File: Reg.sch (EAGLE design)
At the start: 12 parts, among them Q1 NPN2SC3422-2, Q2 NPN2SC3325, Q3 PNP2SA1313

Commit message: 完成
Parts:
- D1: value RED -> SHORT
- D2: value BLUE -> SHORT
- D3, D4: value (none) -> BLUE
- R1, R4: value 1k -> 1.5k
- R2: value DNP -> 1.5k
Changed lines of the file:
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@@
 <part name="Q2" library="my_ic" deviceset="NPN" device="2SC3325"/>
 <part name="JP1" library="pinhead" library_urn="urn:adsk.eagle:library:325" deviceset="PINHD-1X3" device="" package3d_urn="urn:adsk.eagle:package:22458/2" value="CON"/>
-<part name="D1" library="my_rcl" deviceset="LED" device="-SMD1608" value="RED"/>
-<part name="D2" library="my_rcl" deviceset="LED" device="-SMD1608" value="BLUE"/>
-<part name="R2" library="my_rcl" deviceset="R" device="-1608" value="DNP"/>
+<part name="D1" library="my_rcl" deviceset="LED" device="-SMD1608" value="SHORT"/>
+<part name="D2" library="my_rcl" deviceset="LED" device="-SMD1608" value="SHORT"/>
+<part name="R2" library="my_rcl" deviceset="R" device="-1608" value="1.5k"/>
 <part name="Q3" library="my_ic" deviceset="PNP" device="2SA1313"/>
-<part name="R1" library="my_rcl" deviceset="R" device="-1608" value="1k"/>
-<part name="R4" library="my_rcl" deviceset="R" device="-1608" value="1k"/>
+<part name="R1" library="my_rcl" deviceset="R" device="-1608" value="1.5k"/>
+<part name="R4" library="my_rcl" deviceset="R" device="-1608" value="1.5k"/>
 <part name="C7" library="my_rcl" deviceset="C" device="-1608" value="100p"/>
-<part name="D3" library="my_rcl" deviceset="LED" device="-SMD1608"/>
-<part name="D4" library="my_rcl" deviceset="LED" device="-SMD1608"/>
+<part name="D3" library="my_rcl" deviceset="LED" device="-SMD1608" value="BLUE"/>
+<part name="D4" library="my_rcl" deviceset="LED" device="-SMD1608" value="BLUE"/>
 </parts>
 <sheets>
@@
 </instance>
 <instance part="D1" gate="G$1" x="15.24" y="5.08" smashed="yes">
-<attribute name="NAME" x="11.176" y="0.508" size="1.778" layer="95" rot="R90"/>
-<attribute name="VALUE" x="10.795" y="5.588" size="1.778" layer="96" rot="R90"/>
+<attribute name="NAME" x="11.176" y="-2.032" size="1.778" layer="95" rot="R90"/>
+<attribute name="VALUE" x="10.795" y="3.048" size="1.778" layer="96" rot="R90"/>
 </instance>
 <instance part="D2" gate="G$1" x="22.86" y="5.08" smashed="yes">
-<attribute name="NAME" x="26.416" y="0.508" size="1.778" layer="95" rot="R90"/>
-<attribute name="VALUE" x="26.035" y="4.318" size="1.778" layer="96" rot="R90"/>
+<attribute name="NAME" x="26.416" y="-2.032" size="1.778" layer="95" rot="R90"/>
+<attribute name="VALUE" x="26.035" y="3.048" size="1.778" layer="96" rot="R90"/>
 </instance>
 <instance part="R2" gate="G$1" x="30.48" y="5.08" smashed="yes" rot="R90">
@@
 </instance>
 <instance part="R1" gate="G$1" x="7.62" y="25.4" smashed="yes" rot="R90">
-<attribute name="NAME" x="6.1214" y="22.86" size="1.778" layer="95" rot="R90"/>
-<attribute name="VALUE" x="10.922" y="21.59" size="1.778" layer="96" rot="R90"/>
+<attribute name="NAME" x="11.2014" y="19.05" size="1.778" layer="95" rot="R90"/>
+<attribute name="VALUE" x="10.922" y="22.86" size="1.778" layer="96" rot="R90"/>
 </instance>
 <instance part="R4" gate="G$1" x="2.54" y="27.94" smashed="yes" rot="R90">
 <attribute name="NAME" x="1.0414" y="24.13" size="1.778" layer="95" rot="R90"/>
-<attribute name="VALUE" x="5.842" y="24.13" size="1.778" layer="96" rot="R90"/>
+<attribute name="VALUE" x="0.762" y="27.94" size="1.778" layer="96" rot="R90"/>
 </instance>
 <instance part="C7" gate="G$1" x="22.86" y="20.32" smashed="yes">

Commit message: チップオンリーも
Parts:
- added Q4: NPN2SC3325, my_ic:NPN2SC3325
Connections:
- net IN: now also Q4.C
- net N$1: now also Q4.B
- net OUT: now also Q4.E
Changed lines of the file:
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@@
 <part name="D3" library="my_rcl" deviceset="LED" device="-SMD1608" value="BLUE"/>
 <part name="D4" library="my_rcl" deviceset="LED" device="-SMD1608" value="BLUE"/>
+<part name="Q4" library="my_ic" deviceset="NPN" device="2SC3325"/>
 </parts>
 <sheets>
@@
 <attribute name="VALUE" x="36.195" y="25.908" size="1.778" layer="96" rot="R90"/>
 </instance>
+<instance part="Q4" gate="G$1" x="15.24" y="40.64" smashed="yes" rot="R90">
+<attribute name="NAME" x="15.24" y="45.72" size="1.778" layer="95" rot="R90"/>
+<attribute name="VALUE" x="17.78" y="45.72" size="1.778" layer="96" rot="R90"/>
+</instance>
 </instances>
 <busses>
@@
 <wire x1="50.8" y1="-7.62" x2="50.8" y2="33.02" width="0.1524" layer="91"/>
 <pinref part="Q1" gate="G$1" pin="E"/>
-<wire x1="20.32" y1="33.02" x2="30.48" y2="33.02" width="0.1524" layer="91"/>
+<wire x1="20.32" y1="33.02" x2="22.86" y2="33.02" width="0.1524" layer="91"/>
 <pinref part="D4" gate="G$1" pin="A"/>
+<wire x1="22.86" y1="33.02" x2="30.48" y2="33.02" width="0.1524" layer="91"/>
 <wire x1="30.48" y1="33.02" x2="50.8" y2="33.02" width="0.1524" layer="91"/>
 <junction x="30.48" y="33.02"/>
+<pinref part="Q4" gate="G$1" pin="E"/>
+<wire x1="20.32" y1="43.18" x2="22.86" y2="43.18" width="0.1524" layer="91"/>
+<wire x1="22.86" y1="43.18" x2="22.86" y2="33.02" width="0.1524" layer="91"/>
+<junction x="22.86" y="33.02"/>
 </segment>
 </net>
@@
 <segment>
 <pinref part="Q1" gate="G$1" pin="C"/>
-<wire x1="10.16" y1="33.02" x2="2.54" y2="33.02" width="0.1524" layer="91"/>
+<wire x1="10.16" y1="33.02" x2="7.62" y2="33.02" width="0.1524" layer="91"/>
+<wire x1="7.62" y1="33.02" x2="2.54" y2="33.02" width="0.1524" layer="91"/>
 <wire x1="2.54" y1="33.02" x2="-15.24" y2="33.02" width="0.1524" layer="91"/>
 <wire x1="-15.24" y1="33.02" x2="-15.24" y2="22.86" width="0.1524" layer="91"/>
@@
 <pinref part="R4" gate="G$1" pin="2"/>
 <junction x="2.54" y="33.02"/>
+<pinref part="Q4" gate="G$1" pin="C"/>
+<wire x1="7.62" y1="33.02" x2="7.62" y2="43.18" width="0.1524" layer="91"/>
+<wire x1="7.62" y1="43.18" x2="10.16" y2="43.18" width="0.1524" layer="91"/>
+<junction x="7.62" y="33.02"/>
 </segment>
 </net>
@@
 <wire x1="5.08" y1="30.48" x2="7.62" y2="30.48" width="0.1524" layer="91"/>
 <junction x="7.62" y="30.48"/>
+<pinref part="Q4" gate="G$1" pin="B"/>
+<wire x1="15.24" y1="38.1" x2="10.16" y2="38.1" width="0.1524" layer="91"/>
+<wire x1="10.16" y1="38.1" x2="10.16" y2="30.48" width="0.1524" layer="91"/>
+<junction x="10.16" y="30.48"/>
 </segment>
 </net>

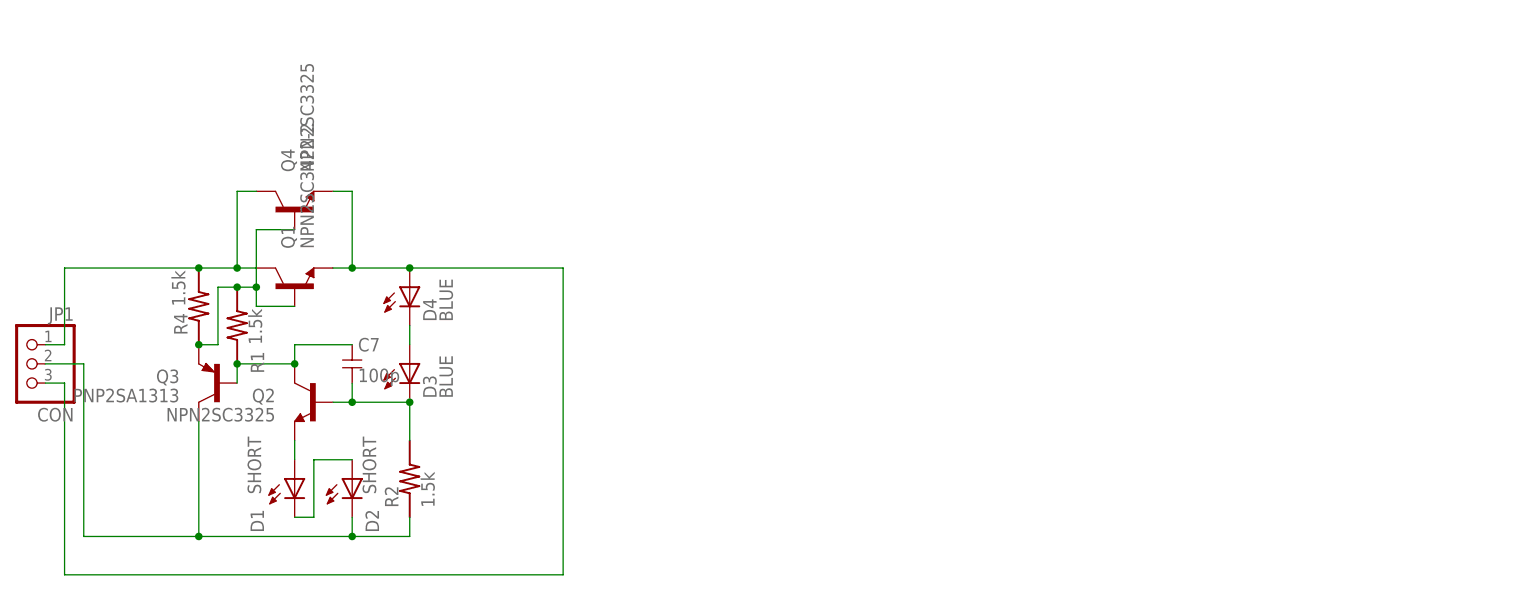
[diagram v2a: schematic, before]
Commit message: ダーリントン、二段増幅を追加
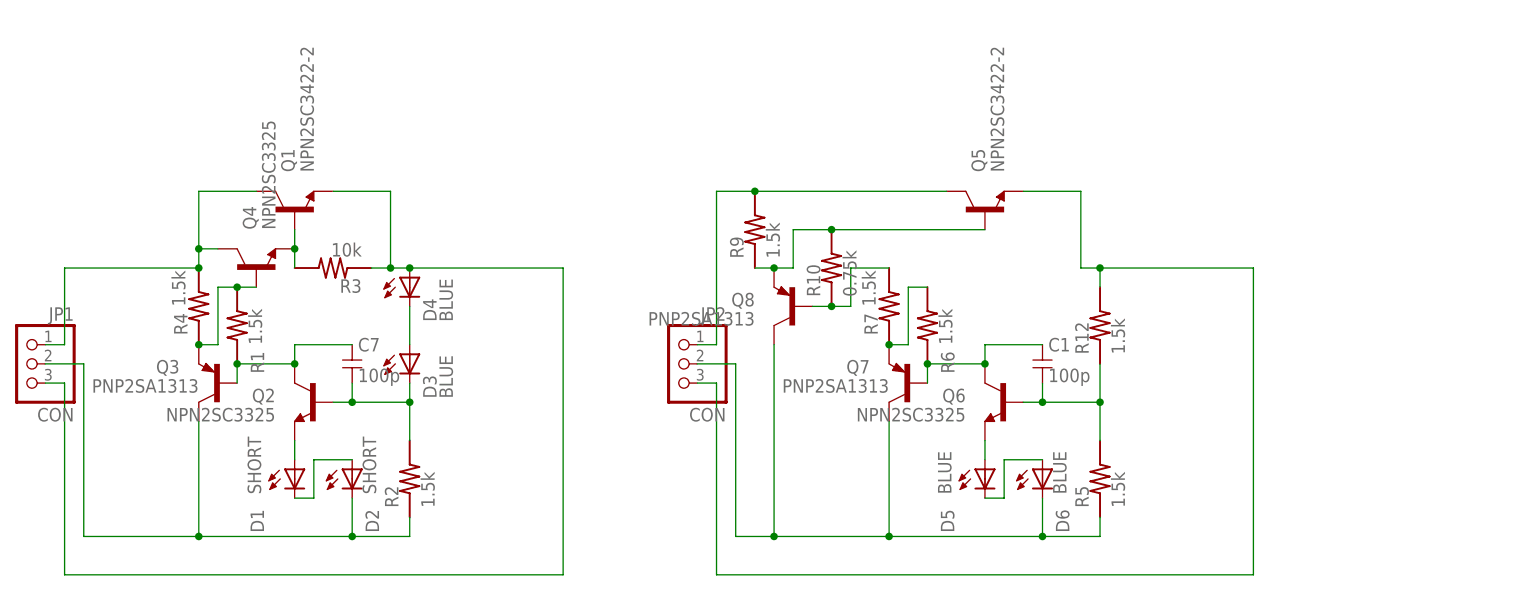
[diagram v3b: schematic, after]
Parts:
- added C1: 100p, my_rcl:C-1608
- added D5, D6: BLUE, my_rcl:LED-SMD1608
- added JP2: CON, pinhead:PINHD-1X3
- added Q5: NPN2SC3422-2, my_ic:NPN2SC3422-2
- added Q6: NPN2SC3325, my_ic:NPN2SC3325
- added Q7, Q8: PNP2SA1313, my_ic:PNP2SA1313
- added R10: 0.75k, my_rcl:R-1608
- added R12, R5, R6, R7, R9: 1.5k, my_rcl:R-1608
- added R3: 10k, my_rcl:R-1608
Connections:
- new net GND1: D6.K, JP2.2, Q7.C, Q8.C, R5.1
- new net IN1: JP2.1, Q5.C, R9.2
- new net N$11: Q7.E, R6.2, R7.1
- new net N$12: C1.1, Q6.C, Q7.B, R6.1
- new net N$13: C1.2, Q6.B, R12.1, R5.2
- new net N$15: Q8.B, R10.1, R7.2
- new net N$16: Q5.B, Q8.E, R10.2, R9.1
- new net N$6: Q1.B, Q4.E, R3.2
- new net N$8: D5.K, D6.A
- new net N$9: D5.A, Q6.E
- new net OUT1: JP2.3, Q5.E, R12.2
- net N$1: no longer Q1.B
- net OUT: now also R3.1; no longer Q4.E
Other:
- moved on the sheet: D1, D2, D3, D4, Q1, Q4

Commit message: 幅を小さくした
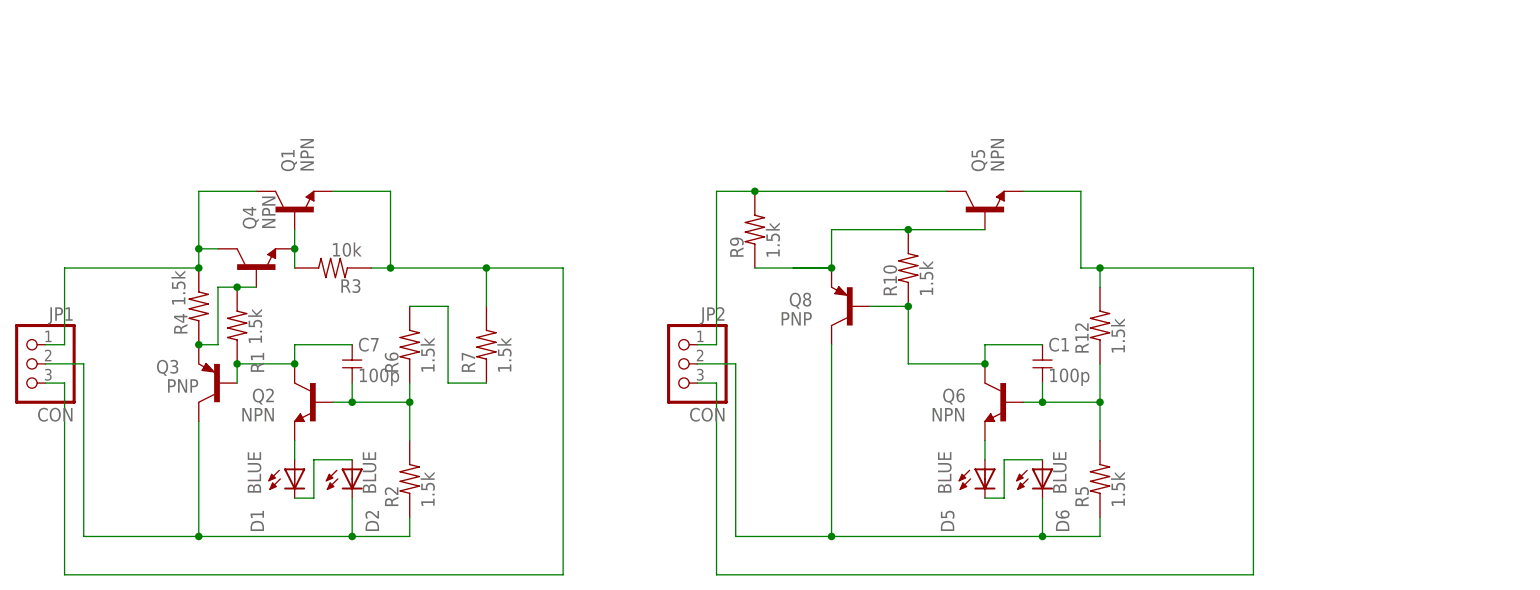
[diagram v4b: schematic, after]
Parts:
- removed D3, D4: BLUE, my_rcl:LED-SMD1608
- removed Q7: PNP2SA1313, my_ic:PNP2SA1313
- D1, D2: value SHORT -> BLUE
- Q1: value NPN2SC3422-2 -> NPN
- Q2, Q4, Q6: value NPN2SC3325 -> NPN
- Q3, Q8: value PNP2SA1313 -> PNP
- Q5: value NPN2SC3422-2 -> NPN; device my_ic:NPN2SC3422-2 -> my_ic:NPN-SOT223
- R10: value 0.75k -> 1.5k
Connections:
- removed net N$11: Q7.E, R6.2, R7.1
- removed net N$15: Q8.B, R10.1, R7.2
- net GND1: no longer Q7.C
- net N$12: now also Q8.B, R10.1; no longer Q7.B, R6.1
- net N$3: now also R6.1; no longer D3.K
- net N$5: now also R6.2, R7.1; no longer D3.A, D4.K
- net OUT: now also R7.2; no longer D4.A
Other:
- moved on the sheet: Q8, R10, R6, R7

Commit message: OPA ver
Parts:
- removed C7: 100p, my_rcl:C-1608
- removed D2, D5, D6: BLUE, my_rcl:LED-SMD1608
- removed JP1: CON, pinhead:PINHD-1X3
- removed Q2, Q4, Q6: NPN, my_ic:NPN2SC3325
- removed Q3, Q8: PNP, my_ic:PNP2SA1313
- removed R10, R12, R4, R5, R6, R7, R9: 1.5k, my_rcl:R-1608
- added C2: 0.1u, my_rcl:C-2012
- added D3: ZENER, my_rcl:ZENER-SMD
- added D4: CRD, my_rcl:CRD-SMD
- added IC1: (no value), my_ic:OPA-2-SOP
- C1: value 100p -> 10p
- D1: value BLUE -> (none); device my_rcl:LED-SMD1608 -> my_rcl:LED-SMD2012
- JP2: device pinhead:PINHD-1X3 -> my_connector:SW-1X3
- Q1: value NPN -> JFET-N; device my_ic:NPN2SC3422-2 -> my_ic:JFET-N
- Q5: device my_ic:NPN-SOT223 -> my_ic:NPN2SC3422-2
- R1, R2: value 1.5k -> 1k
- R3: value 10k -> 1k
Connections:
- removed net GND: D2.K, JP1.2, Q3.C, R2.1
- removed net IN: JP1.1, Q1.C, Q4.C, R4.2
- removed net N$10: C7.1, Q2.C, Q3.B, R1.1
- removed net N$12: C1.1, Q6.C, Q8.B, R10.1
- removed net N$13: C1.2, Q6.B, R12.1, R5.2
- removed net N$16: Q5.B, Q8.E, R10.2, R9.1
- removed net N$6: Q1.B, Q4.E, R3.2
- removed net N$8: D5.K, D6.A
- removed net N$9: D5.A, Q6.E
- removed net OUT: JP1.3, Q1.E, R3.1, R7.2
- net GND1: now also C2.2, D1.K, IC1G$2.+IN, IC1G$3.V-, R1.1; no longer D6.K, Q8.C, R5.1
- net IN1: now also D4.A, Q1.D; no longer R9.2
- net N$1: now also C2.1, D1.A, IC1G$1.+IN, R3.1; no longer Q3.E, Q4.B, R1.2, R4.1
- net N$2: now also D3.C, D4.K, Q1.G, Q1.S, Q5.B; no longer D1.K, D2.A
- net N$3: now also C1.2, IC1G$1.-IN, R1.2, R2.1; no longer C7.2, Q2.B, R2.2, R6.1
- net N$4: now also C1.1, D3.A, IC1G$1.OUT; no longer D1.A, Q2.E
- net N$5: now also IC1G$2.-IN, IC1G$2.OUT; no longer R6.2, R7.1
- net OUT1: now also IC1G$3.V+, R2.2, R3.2; no longer R12.2
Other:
- moved on the sheet: C1, D1, Q5, R1, R2, R3
